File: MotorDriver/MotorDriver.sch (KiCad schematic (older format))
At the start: 8 parts, among them J11 USART, J5 IdSelect, J6 ST_LINK, J7 Hall

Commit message: Finished printable parts
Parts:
- added C20, C21, C22: 10n, Capacitor_SMD:C_0603_1608Metric_Pad1.05x0.95mm_HandSolder, symbol Device:C
- added C23: 100n, Capacitor_SMD:C_0603_1608Metric_Pad1.05x0.95mm_HandSolder, symbol Device:C
- added D5: MRA4003T3G, Diode_SMD:D_SMA-SMB_Universal_Handsoldering, symbol Device:D
- added R19, R20: 100, Resistor_SMD:R_0603_1608Metric_Pad1.05x0.95mm_HandSolder, symbol Device:R
- added R21, R22, R23: 3k3, Resistor_SMD:R_0603_1608Metric_Pad1.05x0.95mm_HandSolder, symbol Device:R
- added R24, R25, R26: 2k2, Resistor_SMD:R_0603_1608Metric_Pad1.05x0.95mm_HandSolder, symbol Device:R
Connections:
- net +3V3: now also R24.1, R25.1, R26.1
- net +5V: now also D5.2 (A); no longer J7.5 (Pin_5)
- net GNDS: now also C20.2, C21.2, C22.2, C23.2
- net procesorová jednotka/HAL_A: now also C20.1, R21.1; no longer J7.4 (Pin_4)
- net procesorová jednotka/HAL_B: now also C21.1, R22.1; no longer J7.3 (Pin_3)
- net procesorová jednotka/HAL_C: now also C22.1, R23.1; no longer J7.2 (Pin_2)
- net procesorová jednotka/USART_RX: now also R20.1; no longer J11.3 (Pin_3)
- net procesorová jednotka/USART_TX: now also R19.1; no longer J11.2 (Pin_2)
- new net: J7.2 (Pin_2), R23.2, R26.2
- new net: J7.3 (Pin_3), R22.2, R25.2
- new net: J7.4 (Pin_4), R21.2, R24.2
- new net: C23.1, D5.1 (K), J7.5 (Pin_5)
- new net: J11.2 (Pin_2), R19.2
- new net: J11.3 (Pin_3), R20.2
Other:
- moved on the sheet: J7

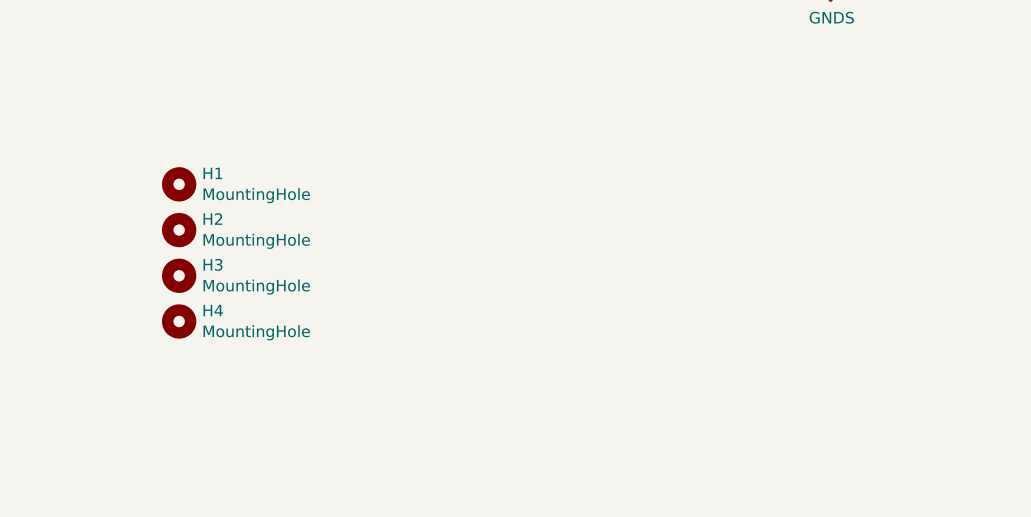
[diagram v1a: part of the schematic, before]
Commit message: Power and output ping changed roblaced by holes. Correction of tracks width and vias diameters.
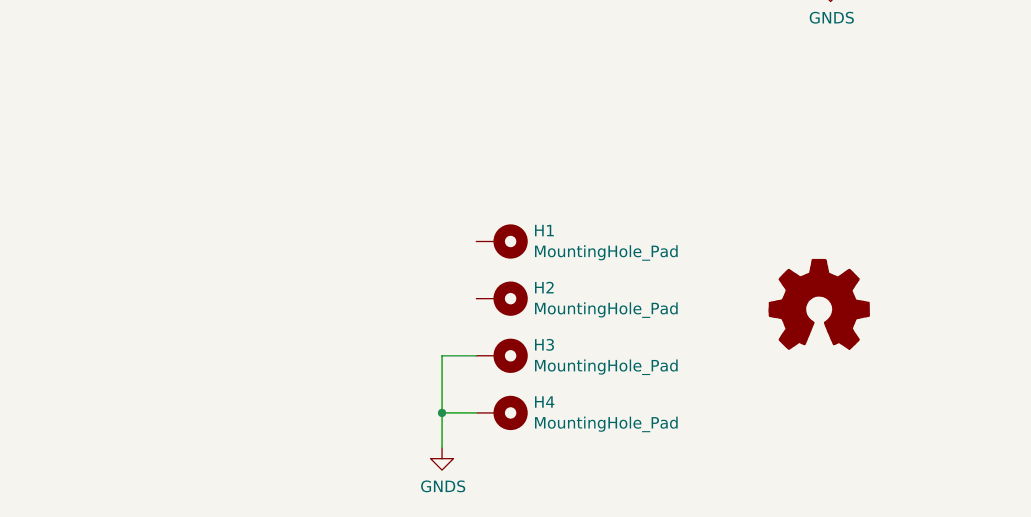
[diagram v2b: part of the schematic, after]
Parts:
- removed H1, H2, H3, H4: MountingHole, MountingHole:MountingHole_3.2mm_M3_ISO7380, symbol Mechanical:MountingHole
- added H1, H2, H3, H4: MountingHole_Pad, MountingHole:MountingHole_3.2mm_M3_Pad, symbol Mechanical:MountingHole_Pad
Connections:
- net GNDS: now also H3.1, H4.1
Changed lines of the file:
@@
 Wire Wire Line
 	4200 1500 4200 1800
-$Comp
-L Mechanical:MountingHole H1
-U 1 1 5C490703
-P 4500 6300
-F 0 "H1" H 4600 6346 50  0000 L CNN
-F 1 "MountingHole" H 4600 6255 50  0000 L CNN
-F 2 "MountingHole:MountingHole_3.2mm_M3_ISO7380" H 4500 6300 50  0001 C CNN
-F 3 "~" H 4500 6300 50  0001 C CNN
-	1    4500 6300
-	1    0    0    -1
-$EndComp
-$Comp
-L Mechanical:MountingHole H2
-U 1 1 5C4907F7
-P 4500 6500
-F 0 "H2" H 4600 6546 50  0000 L CNN
-F 1 "MountingHole" H 4600 6455 50  0000 L CNN
-F 2 "MountingHole:MountingHole_3.2mm_M3_ISO7380" H 4500 6500 50  0001 C CNN
-F 3 "~" H 4500 6500 50  0001 C CNN
-	1    4500 6500
-	1    0    0    -1
-$EndComp
-$Comp
-L Mechanical:MountingHole H3
-U 1 1 5C49085D
-P 4500 6700
-F 0 "H3" H 4600 6746 50  0000 L CNN
-F 1 "MountingHole" H 4600 6655 50  0000 L CNN
-F 2 "MountingHole:MountingHole_3.2mm_M3_ISO7380" H 4500 6700 50  0001 C CNN
-F 3 "~" H 4500 6700 50  0001 C CNN
-	1    4500 6700
-	1    0    0    -1
-$EndComp
-$Comp
-L Mechanical:MountingHole H4
-U 1 1 5C49088B
-P 4500 6900
-F 0 "H4" H 4600 6946 50  0000 L CNN
-F 1 "MountingHole" H 4600 6855 50  0000 L CNN
-F 2 "MountingHole:MountingHole_3.2mm_M3_ISO7380" H 4500 6900 50  0001 C CNN
-F 3 "~" H 4500 6900 50  0001 C CNN
-	1    4500 6900
-	1    0    0    -1
-$EndComp
 Wire Wire Line
 	8800 5000 8800 5100
@@
 Wire Wire Line
 	8800 4200 8800 4600
+$Comp
+L Graphic:Logo_Open_Hardware_Small #LOGO1
+U 1 1 5C4BBF9D
+P 7300 6850
+F 0 "#LOGO1" H 7300 7125 50  0001 C CNN
+F 1 "Logo_Open_Hardware_Small" H 7300 6625 50  0001 C CNN
+F 2 "" H 7300 6850 50  0001 C CNN
+F 3 "~" H 7300 6850 50  0001 C CNN
+	1    7300 6850
+	1    0    0    -1
+$EndComp
+$Comp
+L Mechanical:MountingHole_Pad H1
+U 1 1 5C4BF10A
+P 5900 6550
+F 0 "H1" V 5854 6700 50  0000 L CNN
+F 1 "MountingHole_Pad" V 5945 6700 50  0000 L CNN
+F 2 "MountingHole:MountingHole_3.2mm_M3_Pad" H 5900 6550 50  0001 C CNN
+F 3 "~" H 5900 6550 50  0001 C CNN
+	1    5900 6550
+	0    1    1    0
+$EndComp
+$Comp
+L Mechanical:MountingHole_Pad H2
+U 1 1 5C4C13A3
+P 5900 6800
+F 0 "H2" V 5854 6950 50  0000 L CNN
+F 1 "MountingHole_Pad" V 5945 6950 50  0000 L CNN
+F 2 "MountingHole:MountingHole_3.2mm_M3_Pad" H 5900 6800 50  0001 C CNN
+F 3 "~" H 5900 6800 50  0001 C CNN
+	1    5900 6800
+	0    1    1    0
+$EndComp
+$Comp
+L Mechanical:MountingHole_Pad H3
+U 1 1 5C4C1400
+P 5900 7050
+F 0 "H3" V 5854 7200 50  0000 L CNN
+F 1 "MountingHole_Pad" V 5945 7200 50  0000 L CNN
+F 2 "MountingHole:MountingHole_3.2mm_M3_Pad" H 5900 7050 50  0001 C CNN
+F 3 "~" H 5900 7050 50  0001 C CNN
+	1    5900 7050
+	0    1    1    0
+$EndComp
+$Comp
+L Mechanical:MountingHole_Pad H4
+U 1 1 5C4C146E
+P 5900 7300
+F 0 "H4" V 5854 7450 50  0000 L CNN
+F 1 "MountingHole_Pad" V 5945 7450 50  0000 L CNN
+F 2 "MountingHole:MountingHole_3.2mm_M3_Pad" H 5900 7300 50  0001 C CNN
+F 3 "~" H 5900 7300 50  0001 C CNN
+	1    5900 7300
+	0    1    1    0
+$EndComp
+$Comp
+L power:GNDS #PWR0160
+U 1 1 5C4C314D
+P 5650 7450
+F 0 "#PWR0160" H 5650 7200 50  0001 C CNN
+F 1 "GNDS" H 5655 7277 50  0000 C CNN
+F 2 "" H 5650 7450 50  0001 C CNN
+F 3 "" H 5650 7450 50  0001 C CNN
+	1    5650 7450
+	1    0    0    -1
+$EndComp
+Wire Wire Line
+	5650 7450 5650 7300
+Wire Wire Line
+	5650 7300 5800 7300
+Wire Wire Line
+	5800 7050 5650 7050
+Wire Wire Line
+	5650 7050 5650 7300
+Connection ~ 5650 7300
 $EndSCHEMATC
